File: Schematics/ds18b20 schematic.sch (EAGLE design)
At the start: 5 parts

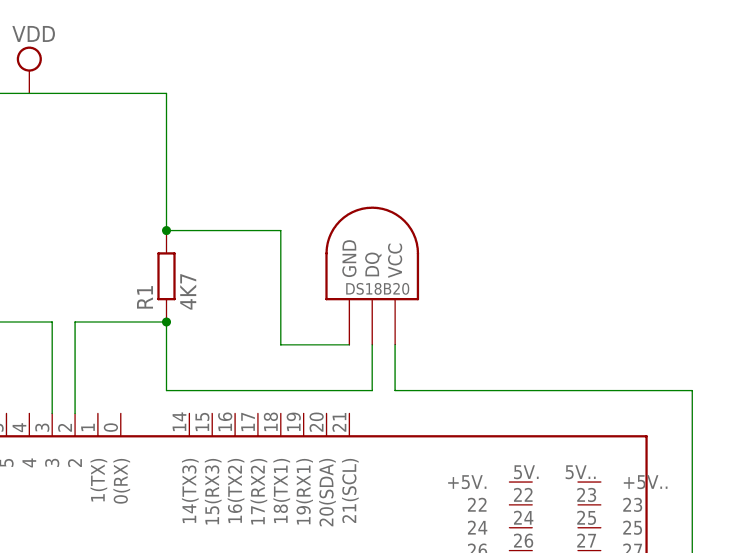
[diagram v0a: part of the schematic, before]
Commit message: rettelse af sensorafsnit, og sidste schematics
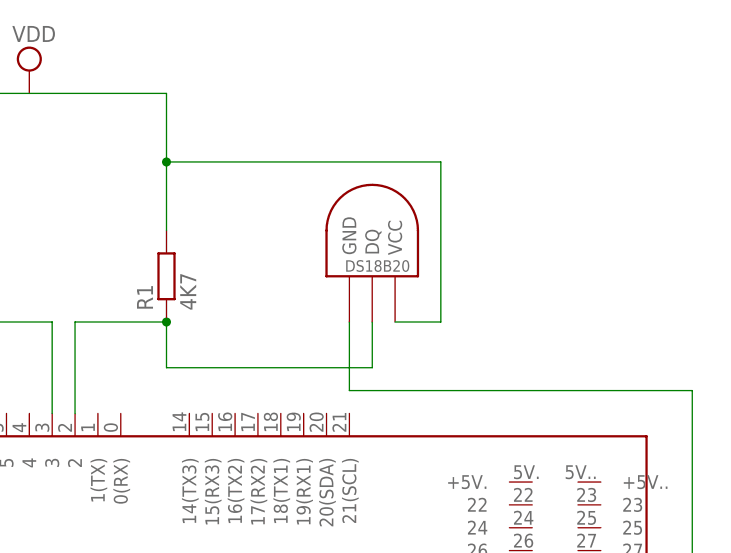
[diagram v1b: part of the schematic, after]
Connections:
- net N$4: now also U$1.GND; no longer U$1.VCC
- net VDD: now also U$1.VCC; no longer U$1.GND
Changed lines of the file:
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@@
 <instance part="R2" gate="G$1" x="0" y="60.96" rot="R90"/>
 <instance part="PCB1" gate="G$1" x="25.4" y="12.7"/>
-<instance part="U$1" gate="G$1" x="55.88" y="53.34"/>
+<instance part="U$1" gate="G$1" x="55.88" y="55.88"/>
 </instances>
 <busses>
@@
 <pinref part="R1" gate="G$1" pin="2"/>
 <wire x1="17.78" y1="76.2" x2="33.02" y2="76.2" width="0.1524" layer="91"/>
-<wire x1="33.02" y1="76.2" x2="33.02" y2="60.96" width="0.1524" layer="91"/>
+<wire x1="33.02" y1="76.2" x2="33.02" y2="68.58" width="0.1524" layer="91"/>
 <pinref part="R2" gate="G$1" pin="2"/>
+<wire x1="33.02" y1="68.58" x2="33.02" y2="60.96" width="0.1524" layer="91"/>
 <wire x1="0" y1="66.04" x2="0" y2="76.2" width="0.1524" layer="91"/>
 <junction x="0" y="76.2"/>
-<wire x1="45.72" y1="60.96" x2="33.02" y2="60.96" width="0.1524" layer="91"/>
-<junction x="33.02" y="60.96"/>
 <pinref part="U$2" gate="G$1" pin="VCC"/>
 <wire x1="-27.94" y1="50.8" x2="-20.32" y2="50.8" width="0.1524" layer="91"/>
 <wire x1="-20.32" y1="50.8" x2="-20.32" y2="53.34" width="0.1524" layer="91"/>
-<wire x1="45.72" y1="60.96" x2="45.72" y2="48.26" width="0.1524" layer="91"/>
-<pinref part="U$1" gate="G$1" pin="GND"/>
-<wire x1="45.72" y1="48.26" x2="53.34" y2="48.26" width="0.1524" layer="91"/>
+<pinref part="U$1" gate="G$1" pin="VCC"/>
+<wire x1="58.42" y1="50.8" x2="63.5" y2="50.8" width="0.1524" layer="91"/>
+<wire x1="63.5" y1="50.8" x2="63.5" y2="68.58" width="0.1524" layer="91"/>
+<wire x1="63.5" y1="68.58" x2="33.02" y2="68.58" width="0.1524" layer="91"/>
+<junction x="33.02" y="68.58"/>
 </segment>
 </net>
@@
 <net name="N$4" class="0">
 <segment>
-<pinref part="U$1" gate="G$1" pin="VCC"/>
-<wire x1="58.42" y1="43.18" x2="58.42" y2="48.26" width="0.1524" layer="91"/>
-<wire x1="58.42" y1="43.18" x2="91.44" y2="43.18" width="0.1524" layer="91"/>
 <wire x1="91.44" y1="43.18" x2="91.44" y2="-20.32" width="0.1524" layer="91"/>
 <pinref part="PCB1" gate="G$1" pin="GND."/>
 <wire x1="91.44" y1="-20.32" x2="5.08" y2="-20.32" width="0.1524" layer="91"/>
 <wire x1="5.08" y1="-20.32" x2="5.08" y2="-17.78" width="0.1524" layer="91"/>
+<wire x1="91.44" y1="43.18" x2="53.34" y2="43.18" width="0.1524" layer="91"/>
+<pinref part="U$1" gate="G$1" pin="GND"/>
+<wire x1="53.34" y1="43.18" x2="53.34" y2="50.8" width="0.1524" layer="91"/>
 </segment>
 </net>
@@
 <pinref part="PCB1" gate="G$1" pin="2"/>
 <pinref part="R1" gate="G$1" pin="1"/>
-<wire x1="33.02" y1="43.18" x2="33.02" y2="50.8" width="0.1524" layer="91"/>
 <wire x1="22.86" y1="50.8" x2="33.02" y2="50.8" width="0.1524" layer="91"/>
+<wire x1="33.02" y1="50.8" x2="33.02" y2="45.72" width="0.1524" layer="91"/>
 <junction x="33.02" y="50.8"/>
 <pinref part="U$1" gate="G$1" pin="DQ"/>
-<wire x1="33.02" y1="43.18" x2="55.88" y2="43.18" width="0.1524" layer="91"/>
-<wire x1="55.88" y1="43.18" x2="55.88" y2="48.26" width="0.1524" layer="91"/>
+<wire x1="33.02" y1="45.72" x2="55.88" y2="45.72" width="0.1524" layer="91"/>
+<wire x1="55.88" y1="45.72" x2="55.88" y2="50.8" width="0.1524" layer="91"/>
 </segment>
 </net>

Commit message: Onewire eksempel
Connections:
- removed net VDD: R1.2, R2.2, U$1.VCC, U$2.VCC
- new net N$1: PCB1.5V, R1.2, R2.2, U$1.VCC, U$2.VCC
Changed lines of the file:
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@@
 <parts>
 <part name="R1" library="resistor" deviceset="R-EU_" device="0204/7" value="4K7"/>
-<part name="ARDUINO5V" library="supply2" deviceset="VDD" device=""/>
 <part name="U$2" library="DHT11" deviceset="DHT11-PION." device=""/>
 <part name="R2" library="resistor" deviceset="R-EU_" device="0204/7" value="5K"/>
@@
 <instances>
 <instance part="R1" gate="G$1" x="33.02" y="55.88" rot="R90"/>
-<instance part="ARDUINO5V" gate="G$1" x="17.78" y="78.74"/>
 <instance part="U$2" gate="G$1" x="-17.78" y="66.04"/>
 <instance part="R2" gate="G$1" x="0" y="60.96" rot="R90"/>
@@
 </busses>
 <nets>
-<net name="VDD" class="0">
-<segment>
-<pinref part="ARDUINO5V" gate="G$1" pin="VDD"/>
-<wire x1="17.78" y1="76.2" x2="0" y2="76.2" width="0.1524" layer="91"/>
-<wire x1="0" y1="76.2" x2="-27.94" y2="76.2" width="0.1524" layer="91"/>
-<wire x1="-27.94" y1="76.2" x2="-27.94" y2="50.8" width="0.1524" layer="91"/>
-<pinref part="R1" gate="G$1" pin="2"/>
-<wire x1="17.78" y1="76.2" x2="33.02" y2="76.2" width="0.1524" layer="91"/>
-<wire x1="33.02" y1="76.2" x2="33.02" y2="68.58" width="0.1524" layer="91"/>
-<pinref part="R2" gate="G$1" pin="2"/>
-<wire x1="33.02" y1="68.58" x2="33.02" y2="60.96" width="0.1524" layer="91"/>
-<wire x1="0" y1="66.04" x2="0" y2="76.2" width="0.1524" layer="91"/>
-<junction x="0" y="76.2"/>
-<pinref part="U$2" gate="G$1" pin="VCC"/>
-<wire x1="-27.94" y1="50.8" x2="-20.32" y2="50.8" width="0.1524" layer="91"/>
-<wire x1="-20.32" y1="50.8" x2="-20.32" y2="53.34" width="0.1524" layer="91"/>
-<pinref part="U$1" gate="G$1" pin="VCC"/>
-<wire x1="58.42" y1="50.8" x2="63.5" y2="50.8" width="0.1524" layer="91"/>
-<wire x1="63.5" y1="50.8" x2="63.5" y2="68.58" width="0.1524" layer="91"/>
-<wire x1="63.5" y1="68.58" x2="33.02" y2="68.58" width="0.1524" layer="91"/>
-<junction x="33.02" y="68.58"/>
-</segment>
-</net>
 <net name="N$2" class="0">
 <segment>
@@
 </segment>
 </net>
+<net name="N$1" class="0">
+<segment>
+<wire x1="33.02" y1="76.2" x2="0" y2="76.2" width="0.1524" layer="91"/>
+<wire x1="0" y1="76.2" x2="-27.94" y2="76.2" width="0.1524" layer="91"/>
+<wire x1="-27.94" y1="76.2" x2="-27.94" y2="50.8" width="0.1524" layer="91"/>
+<pinref part="R1" gate="G$1" pin="2"/>
+<wire x1="33.02" y1="76.2" x2="33.02" y2="68.58" width="0.1524" layer="91"/>
+<pinref part="R2" gate="G$1" pin="2"/>
+<wire x1="33.02" y1="68.58" x2="33.02" y2="60.96" width="0.1524" layer="91"/>
+<wire x1="0" y1="66.04" x2="0" y2="76.2" width="0.1524" layer="91"/>
+<junction x="0" y="76.2"/>
+<pinref part="U$2" gate="G$1" pin="VCC"/>
+<wire x1="-27.94" y1="50.8" x2="-20.32" y2="50.8" width="0.1524" layer="91"/>
+<wire x1="-20.32" y1="50.8" x2="-20.32" y2="53.34" width="0.1524" layer="91"/>
+<pinref part="U$1" gate="G$1" pin="VCC"/>
+<wire x1="58.42" y1="50.8" x2="63.5" y2="50.8" width="0.1524" layer="91"/>
+<wire x1="63.5" y1="50.8" x2="63.5" y2="68.58" width="0.1524" layer="91"/>
+<wire x1="63.5" y1="68.58" x2="33.02" y2="68.58" width="0.1524" layer="91"/>
+<junction x="33.02" y="68.58"/>
+<wire x1="-27.94" y1="76.2" x2="-45.72" y2="76.2" width="0.1524" layer="91"/>
+<wire x1="-45.72" y1="76.2" x2="-45.72" y2="-22.86" width="0.1524" layer="91"/>
+<junction x="-27.94" y="76.2"/>
+<pinref part="PCB1" gate="G$1" pin="5V"/>
+<wire x1="-45.72" y1="-22.86" x2="0" y2="-22.86" width="0.1524" layer="91"/>
+<wire x1="0" y1="-22.86" x2="0" y2="-17.78" width="0.1524" layer="91"/>
+</segment>
+</net>
